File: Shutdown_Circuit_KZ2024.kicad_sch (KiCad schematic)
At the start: 29 parts, among them K1 Relay_DPST-NO, K2 Relay_DPST-NO, K3 Relay_DPST-NO

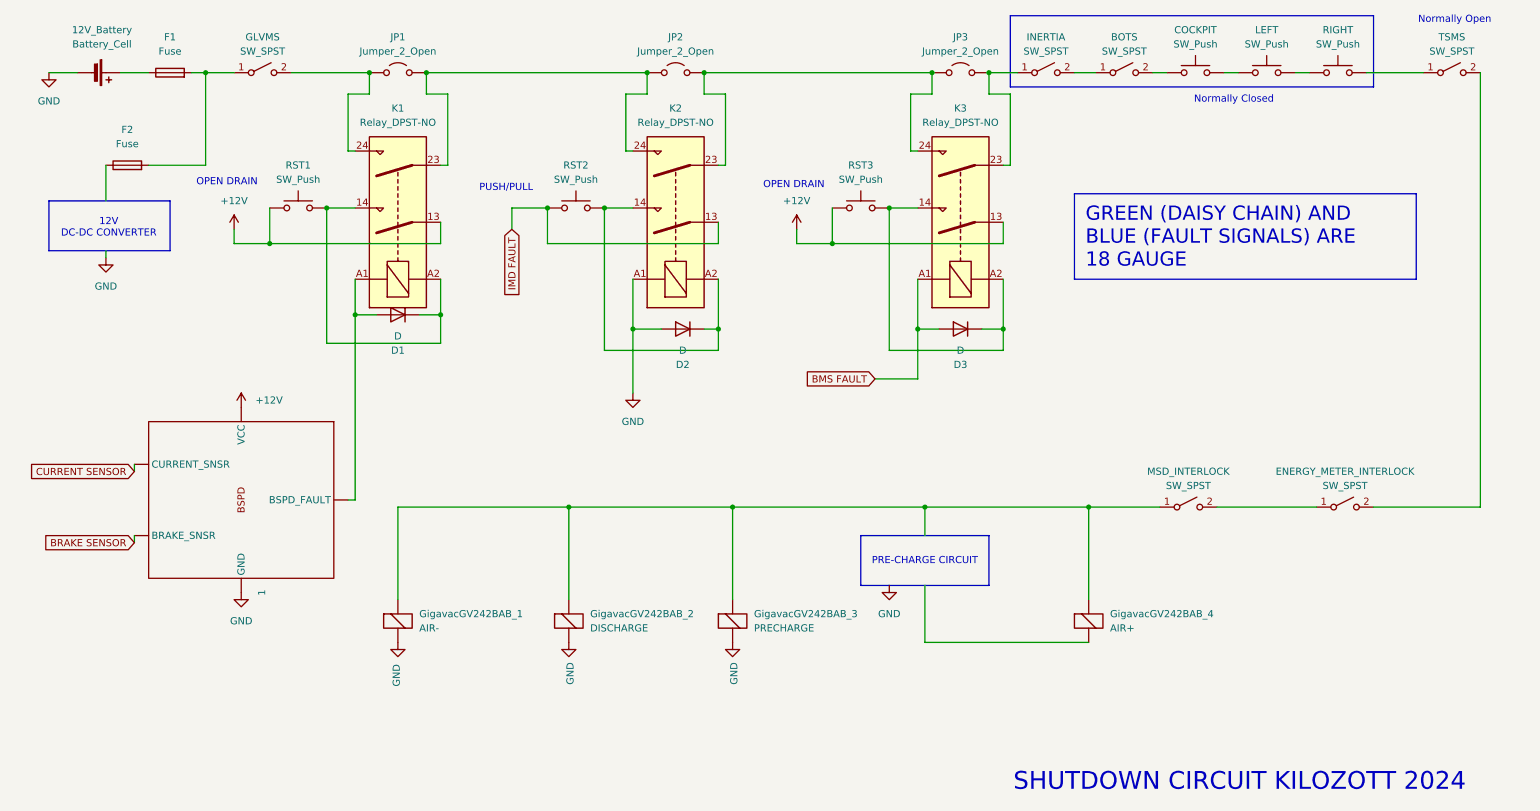
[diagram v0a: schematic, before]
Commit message: added TS interlocks
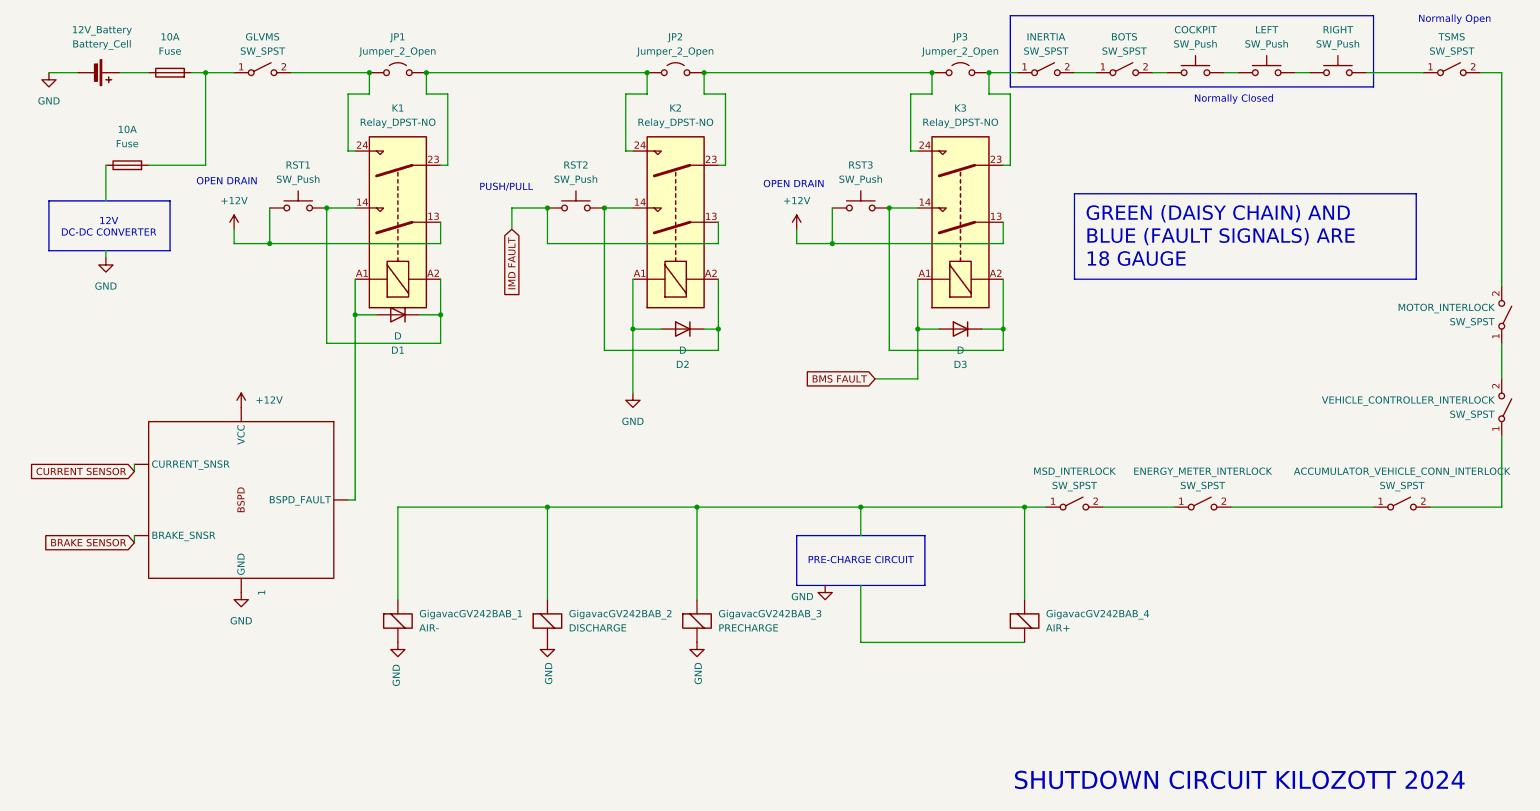
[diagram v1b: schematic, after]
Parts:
- added ACCUMULATOR_VEHICLE_CONN_INTERLOCK, MOTOR_INTERLOCK, VEHICLE_CONTROLLER_INTERLOCK: SW_SPST, symbol Switch:SW_SPST
- renumbered F1 to 10A, F2 to 10A
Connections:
- net at ENERGY_METER_INTERLOCK.2 (B): now also ACCUMULATOR_VEHICLE_CONN_INTERLOCK.1 (A); no longer TSMS.2 (B)
- new net: ACCUMULATOR_VEHICLE_CONN_INTERLOCK.2 (B), VEHICLE_CONTROLLER_INTERLOCK.1 (A)
- new net: MOTOR_INTERLOCK.1 (A), VEHICLE_CONTROLLER_INTERLOCK.2 (B)
- new net: MOTOR_INTERLOCK.2 (B), TSMS.2 (B)
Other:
- moved on the sheet: ENERGY_METER_INTERLOCK, GigavacGV242BAB_2, GigavacGV242BAB_3, GigavacGV242BAB_4, MSD_INTERLOCK
